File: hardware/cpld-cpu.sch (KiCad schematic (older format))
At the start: 392 parts, among them J1 Acc, J10 Page, J11 PC_H, J12 Conn_02x16_Odd_Even, J13 Page, J14 Conn_02x17_Odd_Even, J2 X, J3 IR, J4 AXM, J5 Dec, J6 AR, J7 ALU, J8 Index, J9 PC_L, SW1 BTN0, SW2 BTN0, SW3 BTN0, U1 Acc, U10 RAM_Page, U11 PC_H, U12 CY62138FV30LL, U13 GPIO_RNG, U2 X, U3 IR, U4 Multiplexer, U5 Decoder, U6 AR, U7 ALU, U8 RAM_Index, U9 PC_L

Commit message: VHDL for mem_index
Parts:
- J14: footprint Pin_Headers:Pin_Header_Straight_2x16_Pitch2.54mm -> Pin_Headers:Pin_Header_Straight_2x17_Pitch2.54mm; symbol Connector_Generic:Conn_02x18_Odd_Even -> Connector_Generic:Conn_02x17_Odd_Even
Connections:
- wire segments 1441 -> 1444
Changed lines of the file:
@@
 Text Label 14000 3450 0    50   ~ 0
 D7
-Wire Bus Line
-	10950 4850 5150 4850
 Entry Wire Line
 	2500 2550 2600 2650
@@
 	11050 7100 12100 7100
 Entry Wire Line
-	14650 7200 14750 7300
-Entry Wire Line
-	14650 7300 14750 7400
-Entry Wire Line
 	14650 7400 14750 7500
 Entry Wire Line
@@
 Wire Wire Line
 	13700 7400 14650 7400
-Wire Wire Line
-	14650 7300 13700 7300
-Wire Wire Line
-	13700 7200 14650 7200
-Text Label 11850 7100 0    50   ~ 0
+Text Label 11850 6500 0    50   ~ 0
 X6
-Text Label 11850 7200 0    50   ~ 0
+Text Label 11850 6600 0    50   ~ 0
 X7
-Text Label 14300 7200 0    50   ~ 0
+Text Label 14300 7400 0    50   ~ 0
 X0
-Text Label 14300 7300 0    50   ~ 0
+Text Label 14300 7500 0    50   ~ 0
 X1
-Text Label 14300 7400 0    50   ~ 0
+Text Label 14300 7600 0    50   ~ 0
 X2
-Text Label 14300 7500 0    50   ~ 0
+Text Label 14300 7700 0    50   ~ 0
 X3
-Text Label 14300 7600 0    50   ~ 0
+Text Label 11850 7100 0    50   ~ 0
 X4
-Text Label 14300 7700 0    50   ~ 0
+Text Label 11850 7200 0    50   ~ 0
 X5
 Wire Bus Line
@@
 Entry Wire Line
 	11300 6300 11400 6400
-Entry Wire Line
-	11300 6400 11400 6500
-Entry Wire Line
-	11300 6500 11400 6600
-Wire Wire Line
-	11400 6600 12100 6600
-Wire Wire Line
-	11400 6500 12100 6500
 Wire Wire Line
 	12100 6400 11400 6400
@@
 	11400 6100 12100 6100
 Wire Wire Line
-	12100 6700 11850 6700
+	12100 6700 11800 6700
 Wire Wire Line
-	11850 6700 11850 6650
+	11800 6700 11800 6650
 Wire Wire Line
-	11850 6650 10200 6650
+	11800 6650 10200 6650
 Entry Wire Line
 	11300 7200 11400 7300
@@
 Text Label 11750 6400 0    50   ~ 0
 ARAM9
-Text Label 11750 6500 0    50   ~ 0
+Text Label 13850 7200 0    50   ~ 0
 ARAM10
-Text Label 11750 6600 0    50   ~ 0
+Text Label 13850 7300 0    50   ~ 0
 ARAM11
 Text Label 11750 7300 0    50   ~ 0
@@
 $EndComp
 Wire Bus Line
-	10050 4750 14750 4750
-Wire Bus Line
-	10950 4850 11300 4850
-Connection ~ 10950 4850
+	10050 4750 10950 4750
 Wire Bus Line
 	6750 850  11600 850
@@
 	26300 7550 26300 7650
 $Comp
-L Connector_Generic:Conn_02x18_Odd_Even J14
+L Connector_Generic:Conn_02x17_Odd_Even J14
 U 1 1 A6EC43A8
-P 25750 9000
-F 0 "J14" H 25800 9917 50  0000 C CNN
-F 1 "Conn_02x17_Odd_Even" H 25800 9826 50  0000 C CNN
-F 2 "Pin_Headers:Pin_Header_Straight_2x16_Pitch2.54mm" H 25750 9000 50  0001 C CNN
-F 3 "~" H 25750 9000 50  0001 C CNN
-	1    25750 9000
+P 25750 9100
+F 0 "J14" H 25800 10017 50  0000 C CNN
+F 1 "Conn_02x17_Odd_Even" H 25800 9926 50  0000 C CNN
+F 2 "Pin_Headers:Pin_Header_Straight_2x17_Pitch2.54mm" H 25750 9100 50  0001 C CNN
+F 3 "~" H 25750 9100 50  0001 C CNN
+	1    25750 9100
 	1    0    0    -1
 $EndComp
@@
 	17350 3600 17350 3700
 Wire Bus Line
-	11300 9150 18800 9150
+	11300 9150 14950 9150
 Wire Wire Line
 	16750 3000 16600 3000
@@
 	18900 2550 19650 2550
 Wire Bus Line
+	5150 4850 11300 4850
+Connection ~ 10950 4750
+Wire Bus Line
+	10950 4750 14750 4750
+Entry Wire Line
+	10950 6400 11050 6500
+Entry Wire Line
+	10950 6500 11050 6600
+Wire Wire Line
+	11050 6500 12100 6500
+Wire Wire Line
+	12100 6600 11050 6600
+Connection ~ 14950 9150
+Wire Bus Line
+	14950 9150 18800 9150
+Entry Wire Line
+	14850 7200 14950 7300
+Entry Wire Line
+	14850 7300 14950 7400
+Wire Wire Line
+	14850 7200 13700 7200
+Wire Wire Line
+	13700 7300 14850 7300
+Text Label 7200 6500 0    50   ~ 0
+CLK
+Wire Wire Line
+	7500 6500 7200 6500
+$Comp
+L power:VCC #PWR0101
+U 1 1 6CFA99B4
+P 22750 15550
+F 0 "#PWR0101" H 22750 15400 50  0001 C CNN
+F 1 "VCC" H 22767 15723 50  0000 C CNN
+F 2 "" H 22750 15550 50  0001 C CNN
+F 3 "" H 22750 15550 50  0001 C CNN
+	1    22750 15550
+	-1   0    0    1
+$EndComp
+$Comp
+L power:GND #PWR0102
+U 1 1 6CFA9CCF
+P 23200 15550
+F 0 "#PWR0102" H 23200 15300 50  0001 C CNN
+F 1 "GND" H 23205 15377 50  0000 C CNN
+F 2 "" H 23200 15550 50  0001 C CNN
+F 3 "" H 23200 15550 50  0001 C CNN
+	1    23200 15550
+	1    0    0    -1
+$EndComp
+$Comp
+L power:PWR_FLAG #FLG0101
+U 1 1 6CFAA7E8
+P 22750 15450
+F 0 "#FLG0101" H 22750 15525 50  0001 C CNN
+F 1 "PWR_FLAG" H 22750 15624 50  0000 C CNN
+F 2 "" H 22750 15450 50  0001 C CNN
+F 3 "~" H 22750 15450 50  0001 C CNN
+	1    22750 15450
+	1    0    0    -1
+$EndComp
+$Comp
+L power:PWR_FLAG #FLG0102
+U 1 1 6CFAAB0A
+P 23200 15450
+F 0 "#FLG0102" H 23200 15525 50  0001 C CNN
+F 1 "PWR_FLAG" H 23200 15624 50  0000 C CNN
+F 2 "" H 23200 15450 50  0001 C CNN
+F 3 "~" H 23200 15450 50  0001 C CNN
+	1    23200 15450
+	1    0    0    -1
+$EndComp
+Wire Wire Line
+	23200 15450 23200 15550
+Wire Wire Line
+	22750 15450 22750 15550
+Wire Bus Line
 	26600 9800 26600 10150
 Wire Wire Line
@@
 	2500 4850 2500 6900
 Wire Bus Line
-	10950 4850 10950 7200
-Wire Bus Line
 	22000 4900 22000 6900
 Wire Bus Line
@@
 	19750 2000 19750 5050
 Wire Bus Line
+	14950 7200 14950 9150
+Wire Bus Line
 	14550 2650 14550 4850
 Wire Bus Line
@@
 	21350 5050 21350 6600
 Wire Bus Line
+	14750 4750 14750 7800
+Wire Bus Line
 	5950 12350 5950 14550
 Wire Bus Line
@@
 	5050 4850 5050 6700
 Wire Bus Line
-	14750 4750 14750 7800
+	10950 4750 10950 7200
 Wire Bus Line
 	15800 4900 15800 6400

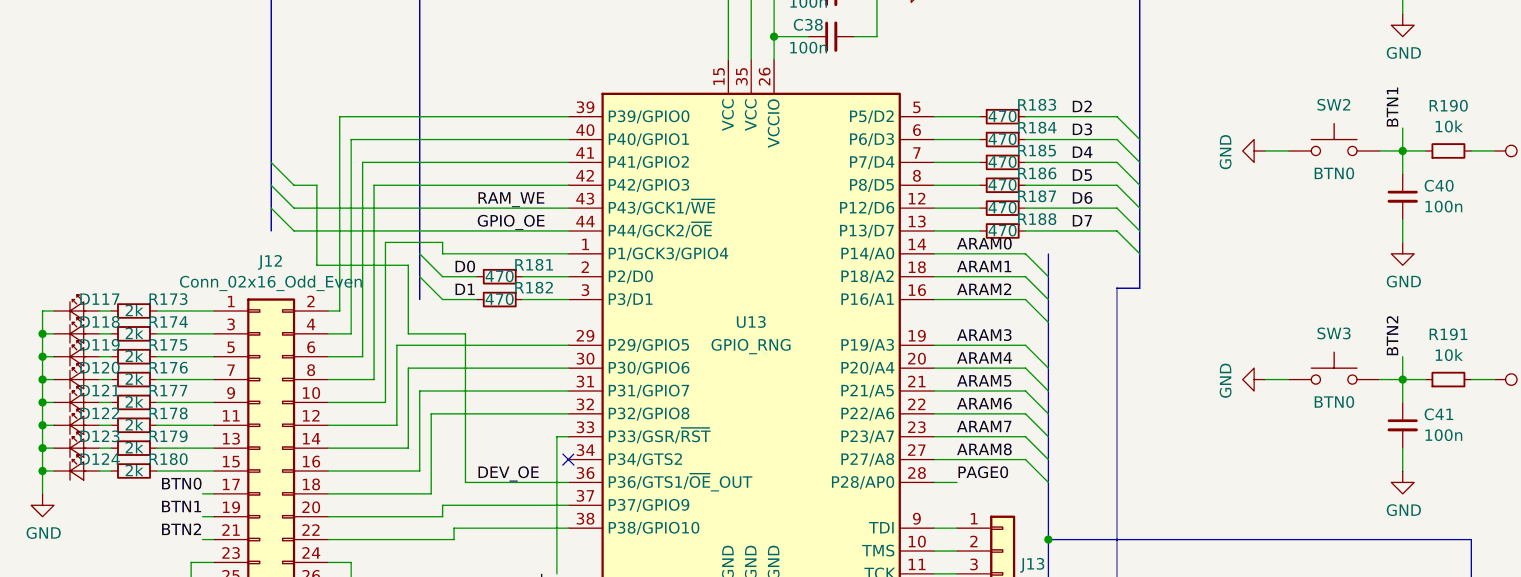
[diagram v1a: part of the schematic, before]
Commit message: Route data bus
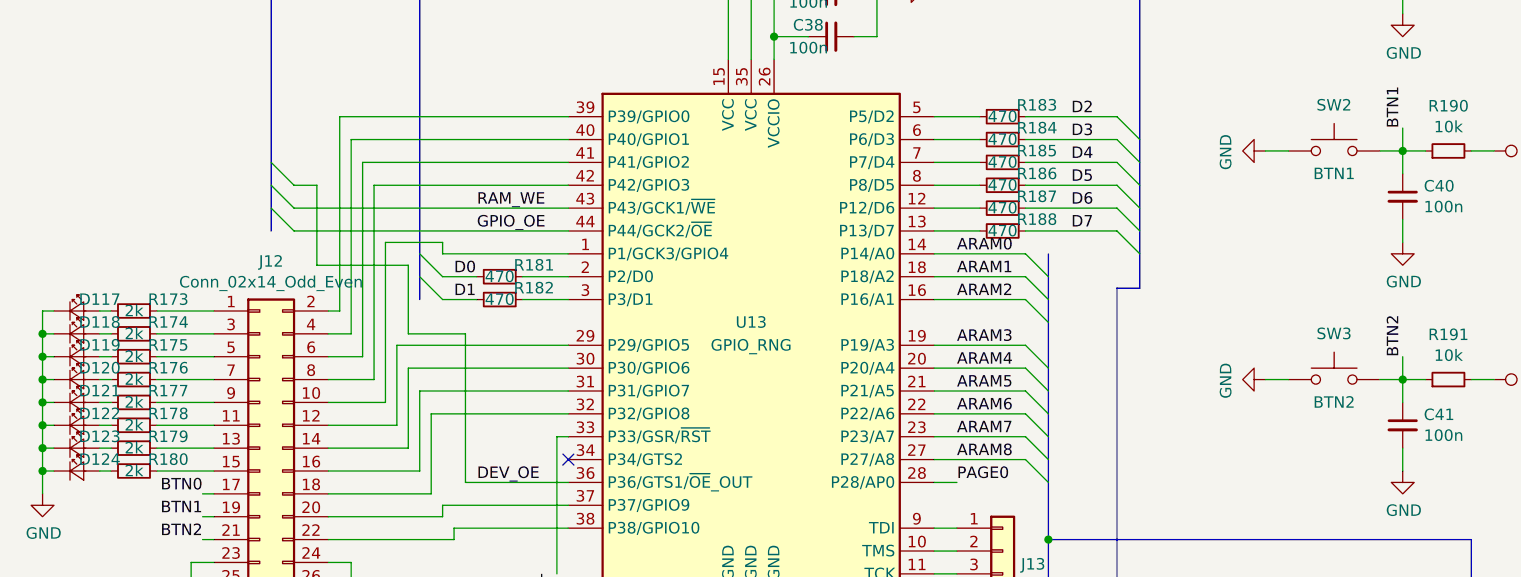
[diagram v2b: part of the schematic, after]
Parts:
- J12: value Conn_02x16_Odd_Even -> Conn_02x14_Odd_Even; footprint Pin_Headers:Pin_Header_Straight_2x16_Pitch2.54mm -> Pin_Headers:Pin_Header_Straight_2x14_Pitch2.54mm
- SW2: value BTN0 -> BTN1
- SW3: value BTN0 -> BTN2
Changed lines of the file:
@@
 P 21300 7550
 F 0 "J12" H 21350 8367 50  0000 C CNN
-F 1 "Conn_02x16_Odd_Even" H 21350 8276 50  0000 C CNN
-F 2 "Pin_Headers:Pin_Header_Straight_2x16_Pitch2.54mm" H 21300 7550 50  0001 C CNN
+F 1 "Conn_02x14_Odd_Even" H 21350 8276 50  0000 C CNN
+F 2 "Pin_Headers:Pin_Header_Straight_2x14_Pitch2.54mm" H 21300 7550 50  0001 C CNN
 F 3 "~" H 21300 7550 50  0001 C CNN
 	1    21300 7550
@@
 P 26000 6250
 F 0 "SW2" H 26000 6450 50  0000 C CNN
-F 1 "BTN0" H 26000 6150 50  0000 C CNN
+F 1 "BTN1" H 26000 6150 50  0000 C CNN
 F 2 "Buttons_Switches_SMD:SW_SPST_B3S-1000" H 26000 6450 50  0001 C CNN
 F 3 "" H 26000 6450 50  0001 C CNN
@@
 P 26000 7250
 F 0 "SW3" H 26000 7450 50  0000 C CNN
-F 1 "BTN0" H 26000 7150 50  0000 C CNN
+F 1 "BTN2" H 26000 7150 50  0000 C CNN
 F 2 "Buttons_Switches_SMD:SW_SPST_B3S-1000" H 26000 7450 50  0001 C CNN
 F 3 "" H 26000 7450 50  0001 C CNN

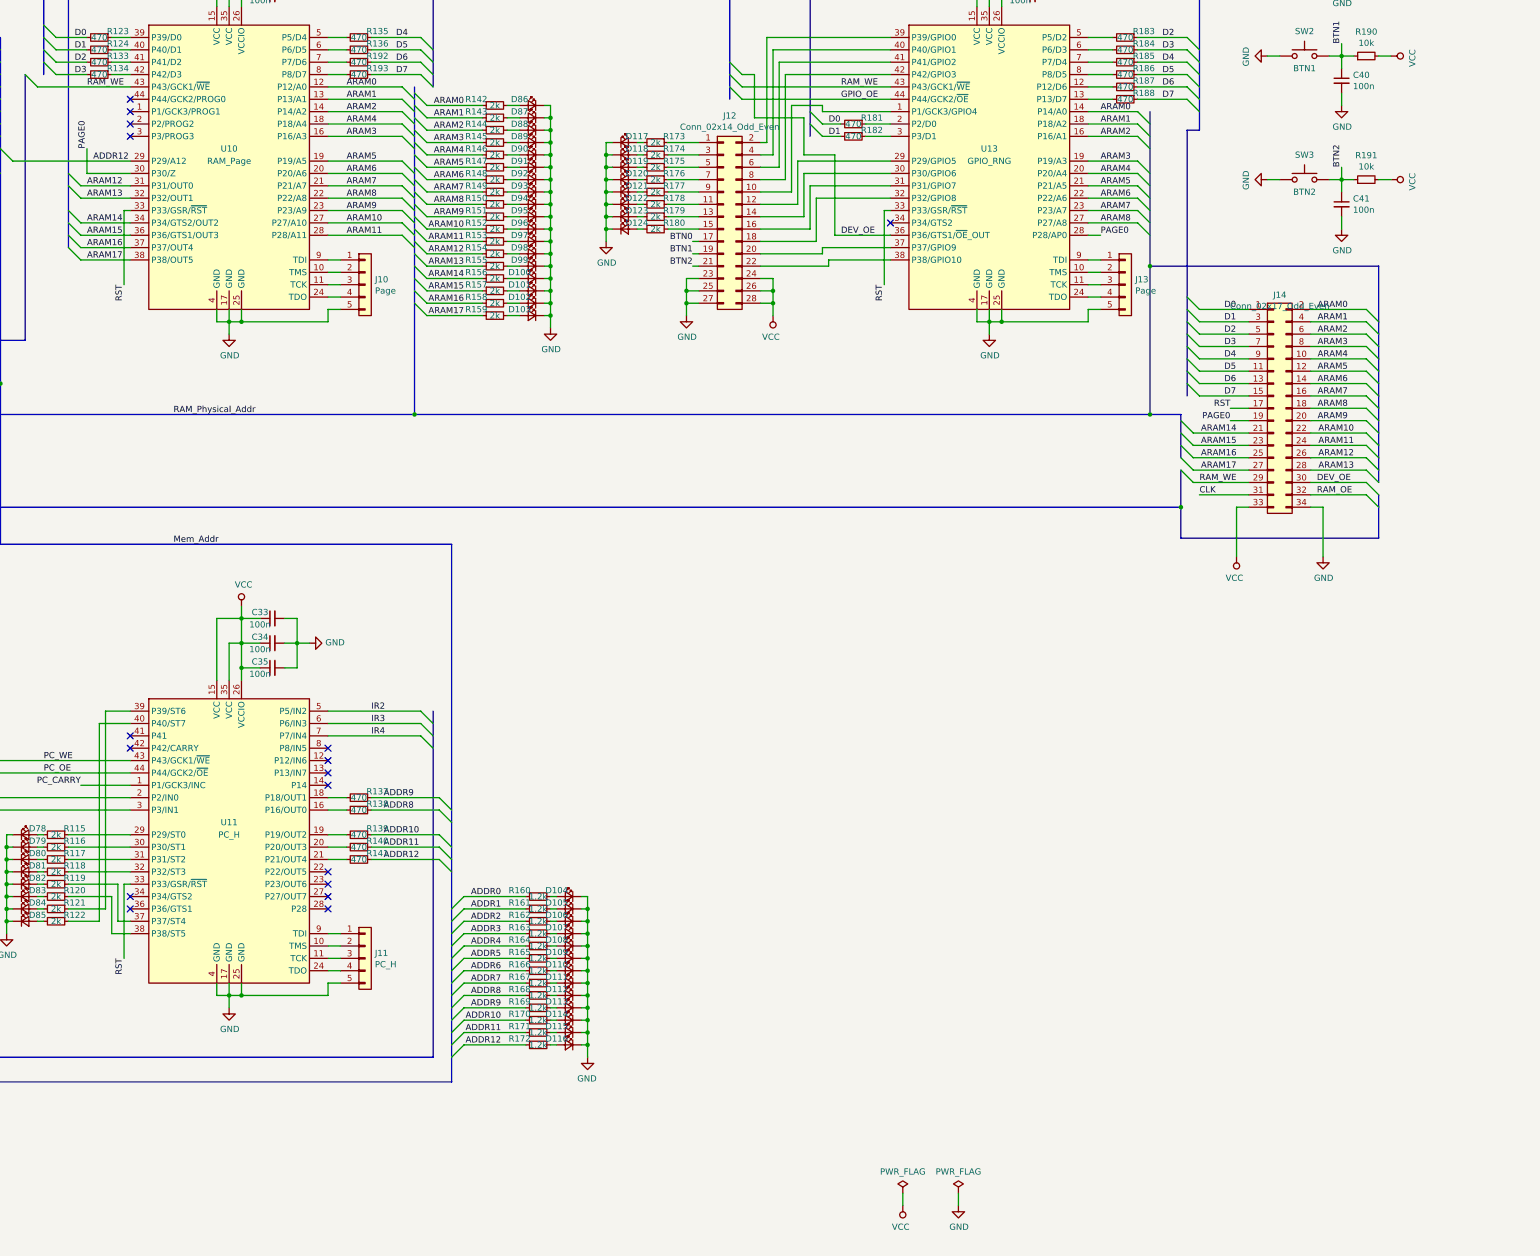
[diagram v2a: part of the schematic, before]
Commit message: Clock schematic
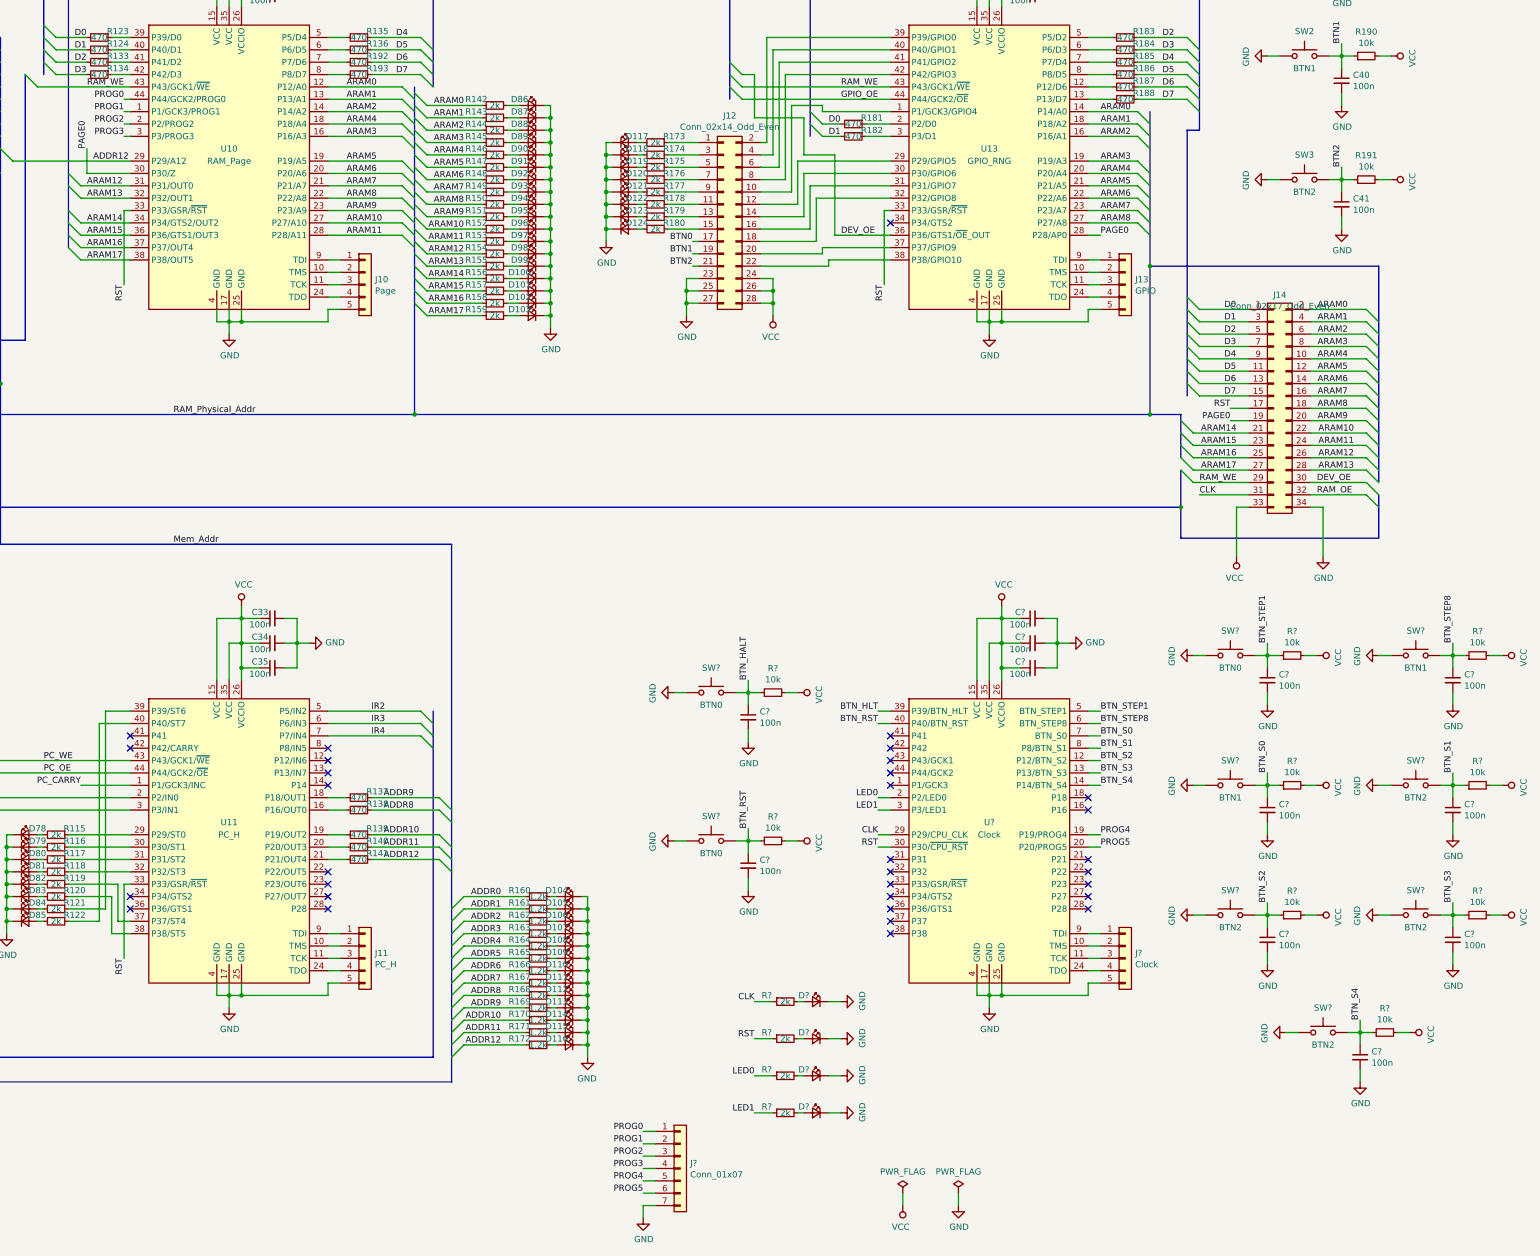
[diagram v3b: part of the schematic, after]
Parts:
- added C? (x12): 100n, Capacitors_SMD:C_0805_HandSoldering, symbol Device:C_Small
- added D? (x4): LED_Small, LEDs:LED_0805_HandSoldering, symbol Device:LED_Small
- added J?: Clock, Pin_Headers:Pin_Header_Straight_1x05_Pitch2.54mm, symbol Connector_Generic:Conn_01x05
- added J?: Conn_01x07, symbol Connector_Generic:Conn_01x07
- added R? (x9): 10k, Resistors_SMD:R_0805_HandSoldering, symbol Device:R_Small
- added R? (x4): 2k, Resistors_SMD:R_0805_HandSoldering, symbol Device:R_Small
- added SW? (x3): BTN0, Buttons_Switches_SMD:SW_SPST_B3S-1000, symbol Switch:SW_Push
- added SW? (x2): BTN1, Buttons_Switches_SMD:SW_SPST_B3S-1000, symbol Switch:SW_Push
- added SW? (x4): BTN2, Buttons_Switches_SMD:SW_SPST_B3S-1000, symbol Switch:SW_Push
- added U?: Clock, Housings_QFP:TQFP-44_10x10mm_Pitch0.8mm, symbol CPLD_CPU_Component:CPLD_CPU_Clock
- J13: value Page -> GPIO
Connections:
- net CLK: now also R?.1, U?.29 (P29/CPU_CLK)
- net GND: now also C?.2, C?.2, C?.2, C?.2, C?.2, C?.2, C?.2, C?.2, C?.2, C?.2, C?.2, C?.2, D?.1 (K), D?.1 (K), D?.1 (K), D?.1 (K), J?.5 (Pin_5), J?.7 (Pin_7), SW?.1, SW?.1, SW?.1, SW?.1, SW?.1, SW?.1, SW?.1, SW?.1, SW?.1, U?.17 (GND), U?.25 (GND), U?.4 (GND)
- net RST: now also R?.1, U?.30 (P30/~CPU_RST~)
- net VCC: now also C?.1, C?.1, C?.1, R?.2, R?.2, R?.2, R?.2, R?.2, R?.2, R?.2, R?.2, R?.2, U?.15 (VCC), U?.26 (VCCIO), U?.35 (VCC)
- net PROG1: now reaches U10.1 (P1/GCK3/PROG1)
- net PROG1: now also J?.2 (Pin_2)
- net PROG2: now reaches U10.2 (P2/PROG2)
- net PROG2: now also J?.3 (Pin_3)
- net PROG3: now reaches U10.3 (P3/PROG3)
- net PROG3: now also J?.4 (Pin_4)
- net PROG0: now reaches U10.44 (P44/GCK2/PROG0)
- net PROG0: now also J?.1 (Pin_1)
- new net: J?.2 (Pin_2), U?.10 (TMS)
- new net: J?.3 (Pin_3), U?.11 (TCK)
- new net: J?.4 (Pin_4), U?.24 (TDO)
- new net: J?.1 (Pin_1), U?.9 (TDI)
- new net: D?.2 (A), R?.2 (x4)
- new net BTN_HALT: C?.1, R?.1, SW?.2
- new net BTN_HLT: U?.39 (P39/BTN_HLT)
- new net BTN_RST: C?.1, R?.1, SW?.2, U?.40 (P40/BTN_RST)
- new net BTN_S0: C?.1, R?.1, SW?.2, U?.7 (BTN_S0)
- new net BTN_S1: C?.1, R?.1, SW?.2, U?.8 (P8/BTN_S1)
- new net BTN_S2: C?.1, R?.1, SW?.2, U?.12 (P12/BTN_S2)
- new net BTN_S3: C?.1, R?.1, SW?.2, U?.13 (P13/BTN_S3)
- new net BTN_S4: C?.1, R?.1, SW?.2, U?.14 (P14/BTN_S4)
- new net BTN_STEP1: C?.1, R?.1, SW?.2, U?.5 (BTN_STEP1)
- new net BTN_STEP8: C?.1, R?.1, SW?.2, U?.6 (BTN_STEP8)
- new net LED0: R?.1, U?.2 (P2/LED0)
- new net LED1: R?.1, U?.3 (P3/LED1)
- new net PROG4: J?.5 (Pin_5), U?.19 (P19/PROG4)
- new net PROG5: J?.6 (Pin_6), U?.20 (P20/PROG5)
- no-connect marks 68 -> 83
